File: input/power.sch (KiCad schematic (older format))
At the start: 61 parts, among them Q2 2STD1665T4, Q3 NSS1C300ET4G, U4 OPA830, U6 OPA830, U7 MCP1755S-3302E/DB, U8 NCP1117STAT3G

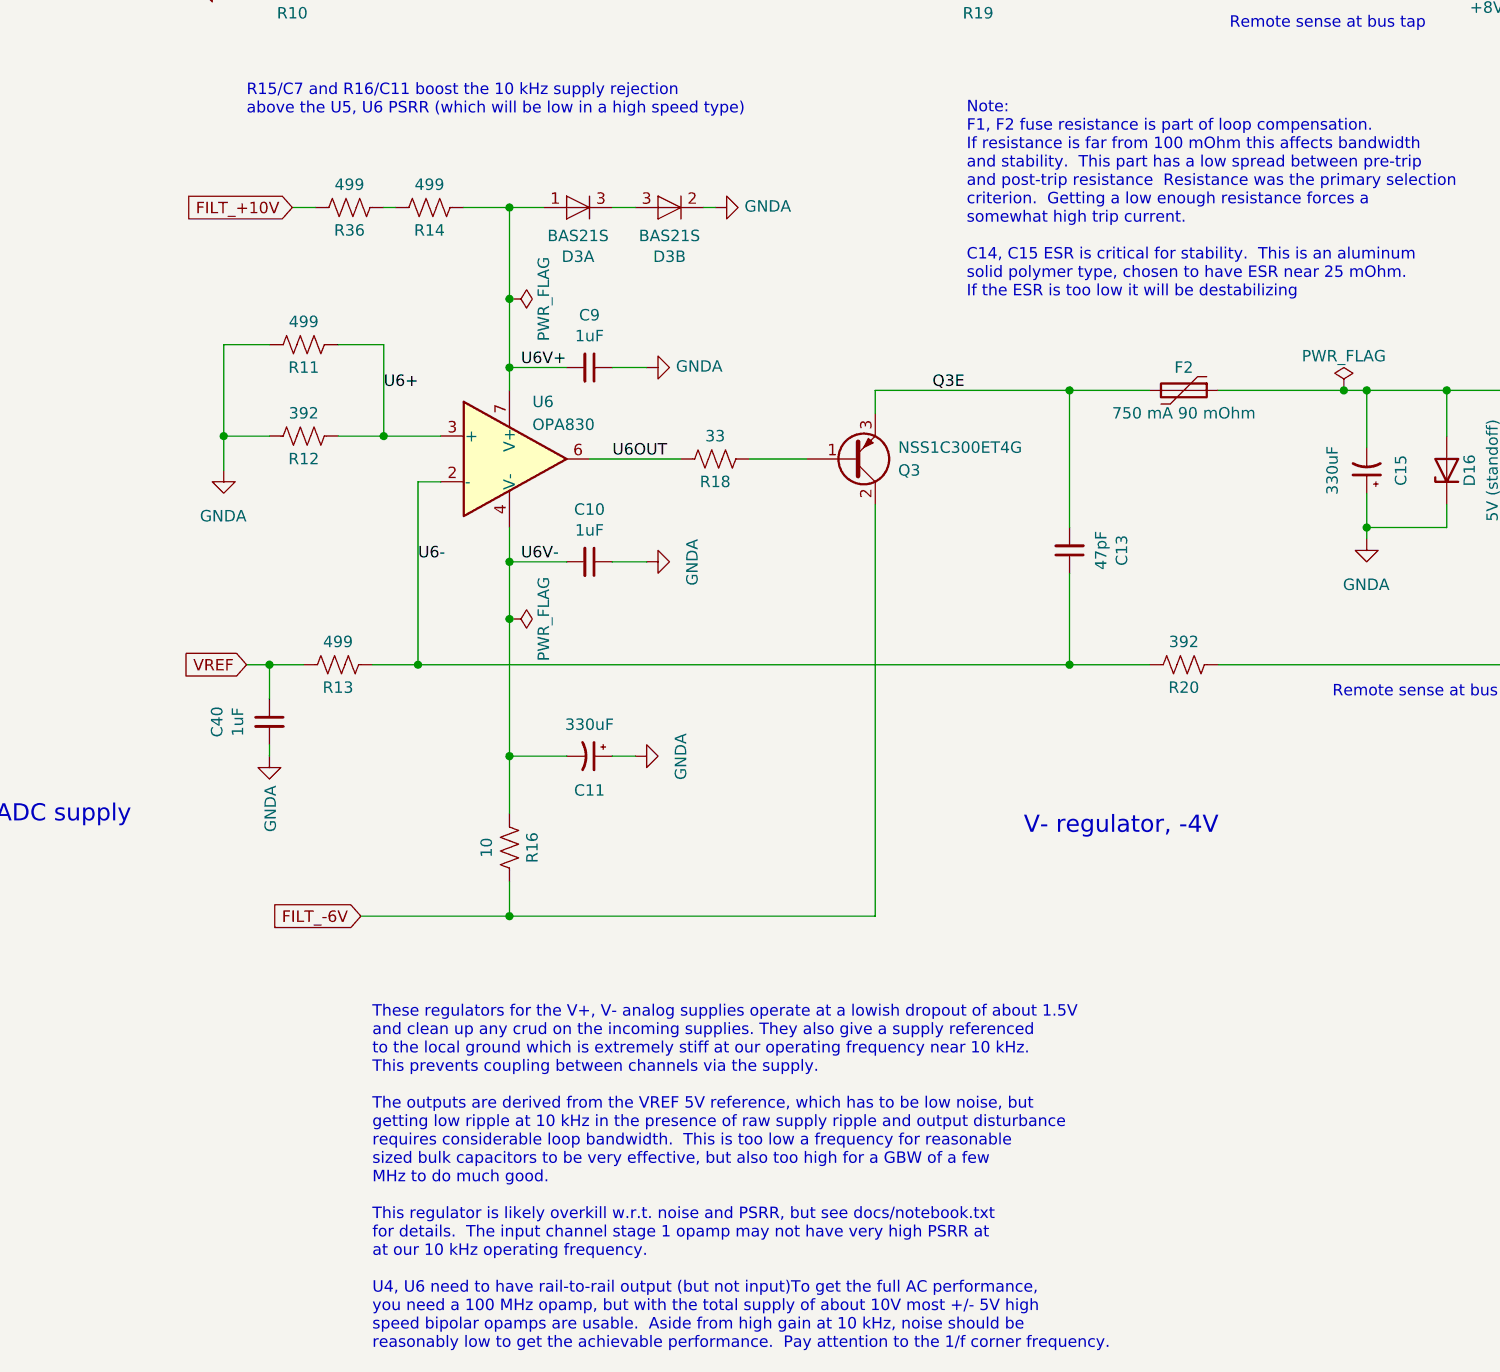
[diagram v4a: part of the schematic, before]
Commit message: Add lowpass filter to input board reference buffer, and fix antialias frequency response. Supply and reference testing in notebook.txt, lots of discussion of reference noise.
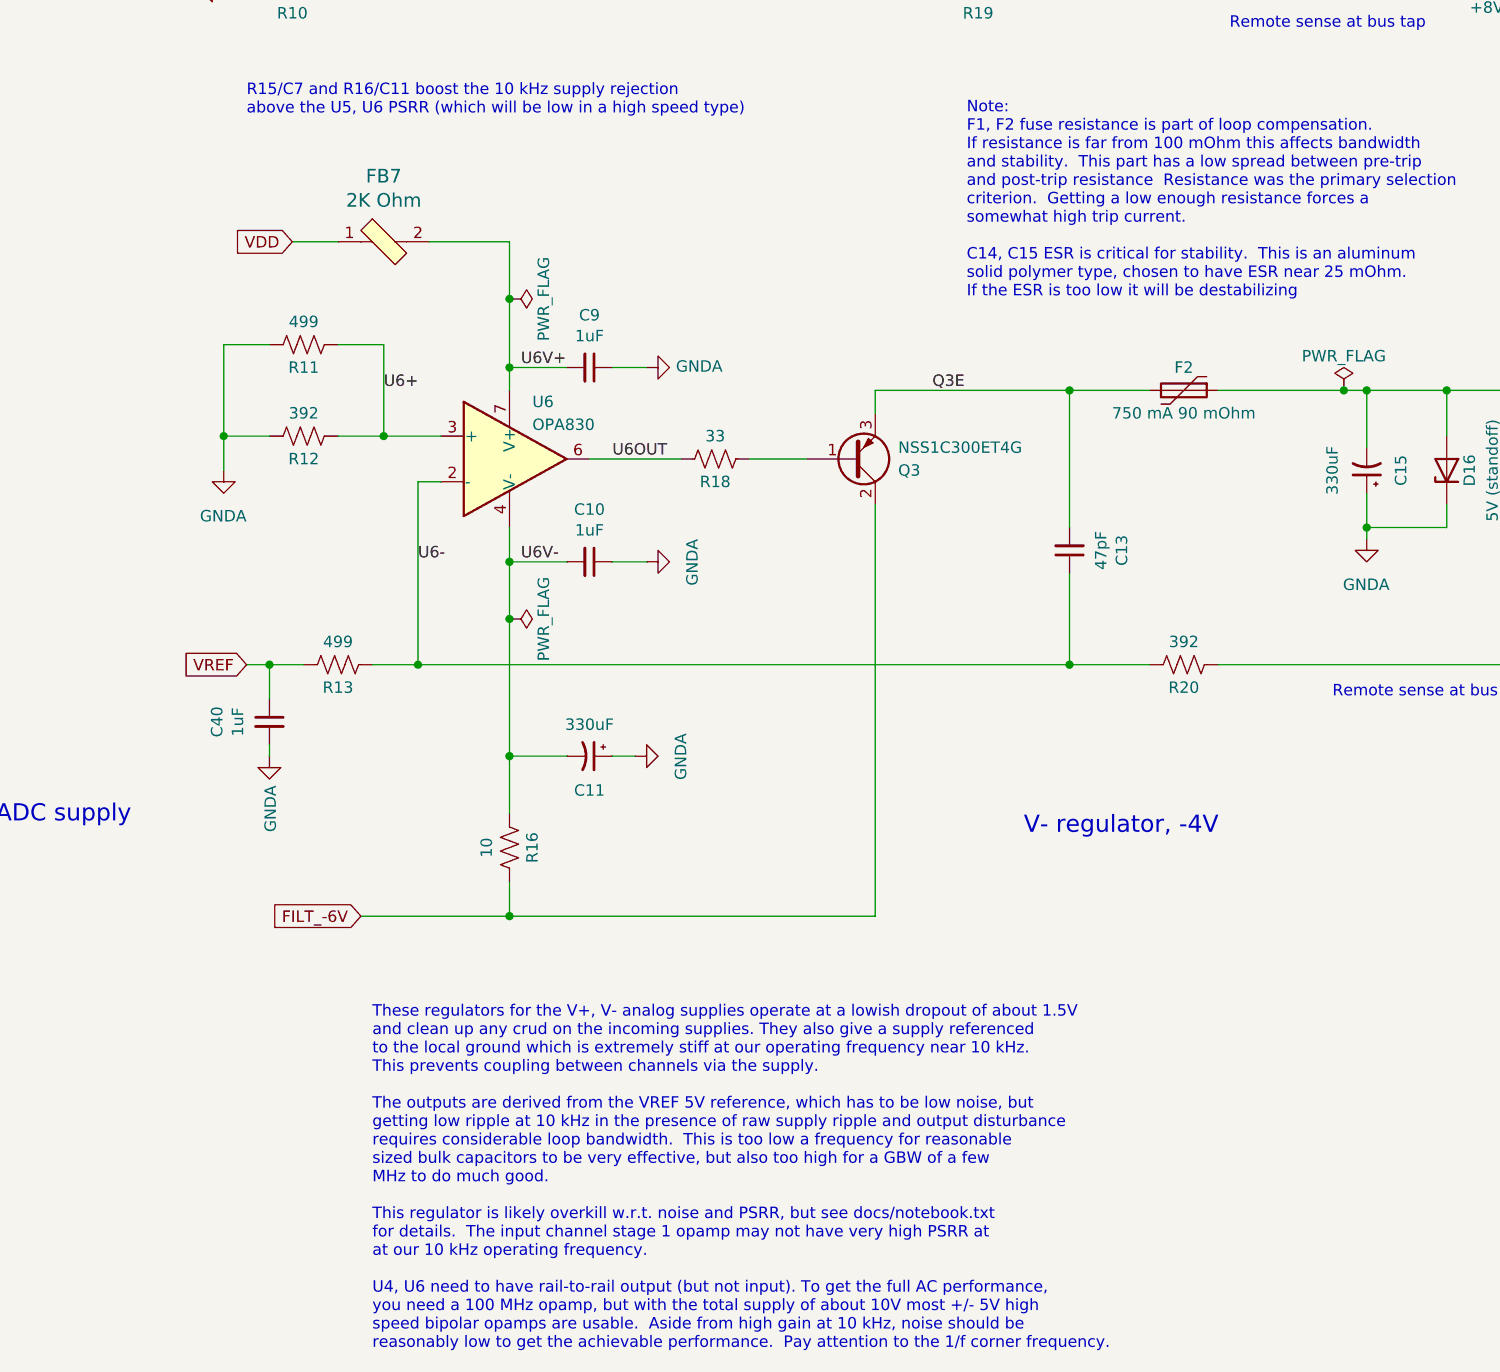
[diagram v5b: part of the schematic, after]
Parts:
- removed D3: BAS21S, Package_TO_SOT_SMD:SOT-23, symbol ilemt_input:BAS21S
- removed R14, R36: 499, Resistor_SMD:R_0805_2012Metric, symbol Device:R_US
- added FB7: 2K Ohm, Inductor_SMD:L_0805_2012Metric, symbol dk_Ferrite-Beads-and-Chips:MPZ2012S601AT000
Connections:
- net U6V+: now also FB7.2
- net VDD: now also FB7.1

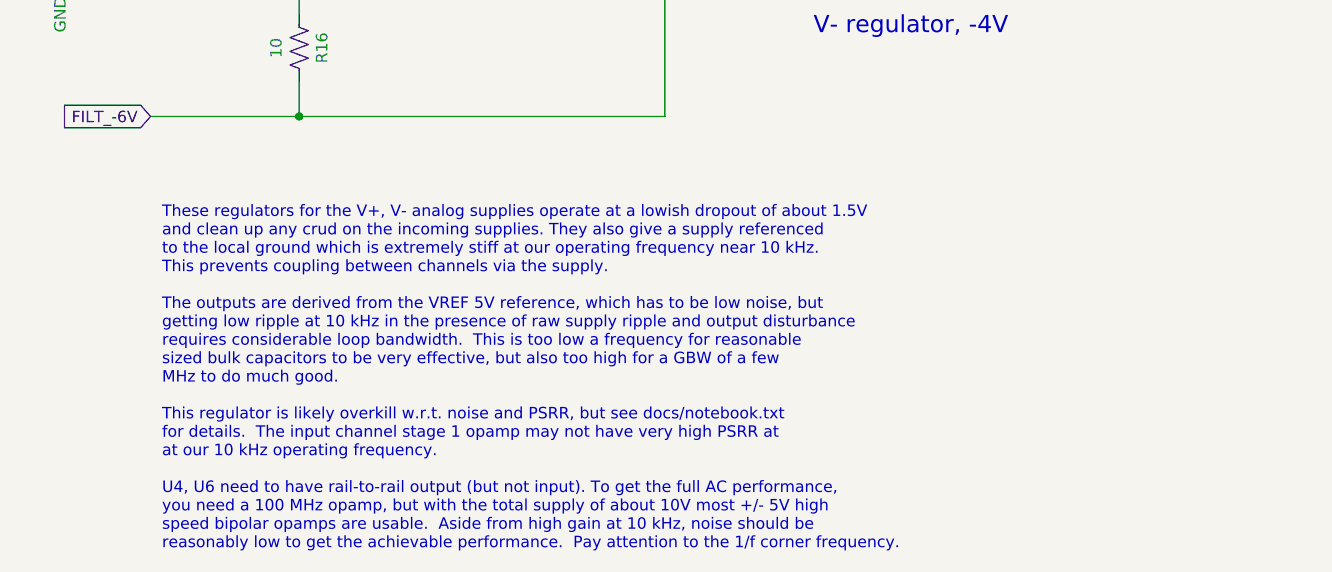
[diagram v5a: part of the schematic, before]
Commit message: notebook.txt and tweaks to comments in input board (no circuit changes).
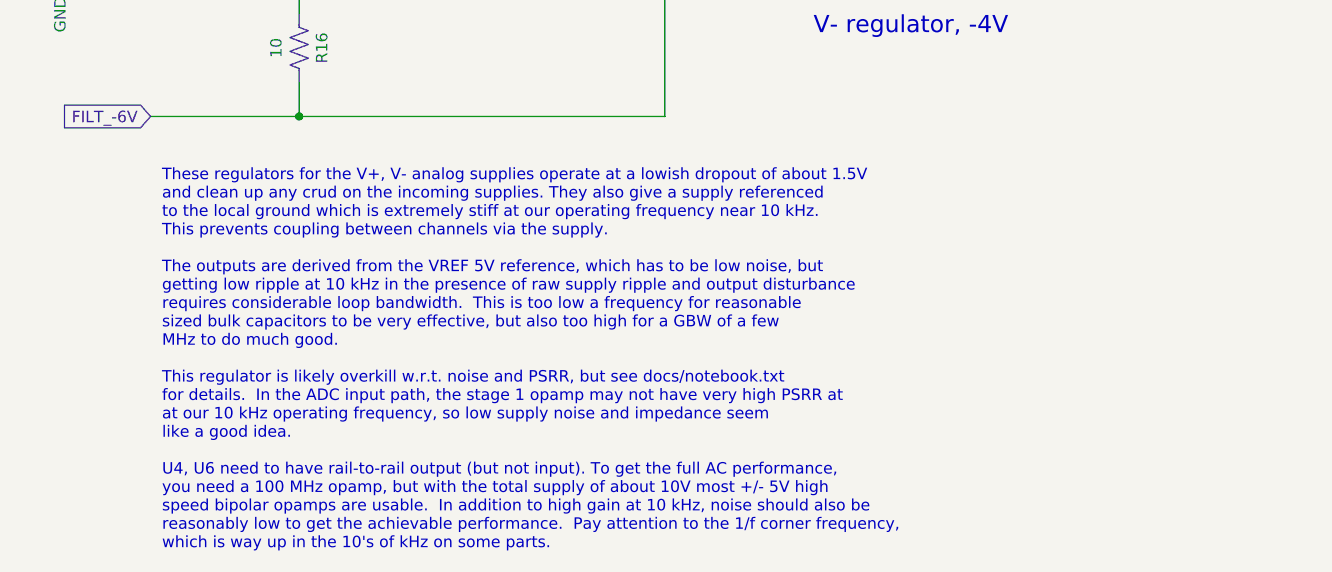
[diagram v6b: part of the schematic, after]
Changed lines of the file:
@@
 $EndComp
 Text Notes 8050 9450 0    50   ~ 0
-These regulators for the V+, V- analog supplies operate at a lowish dropout of about 1.5V\nand clean up any crud on the incoming supplies. They also give a supply referenced\nto the local ground which is extremely stiff at our operating frequency near 10 kHz.\nThis prevents coupling between channels via the supply. \n\nThe outputs are derived from the VREF 5V reference, which has to be low noise, but \ngetting low ripple at 10 kHz in the presence of raw supply ripple and output disturbance\nrequires considerable loop bandwidth.  This is too low a frequency for reasonable\nsized bulk capacitors to be very effective, but also too high for a GBW of a few\nMHz to do much good.\n\nThis regulator is likely overkill w.r.t. noise and PSRR, but see docs/notebook.txt\nfor details.  The input channel stage 1 opamp may not have very high PSRR at\nat our 10 kHz operating frequency.\n\nU4, U6 need to have rail-to-rail output (but not input). To get the full AC performance, \nyou need a 100 MHz opamp, but with the total supply of about 10V most +/- 5V high \nspeed bipolar opamps are usable.  Aside from high gain at 10 kHz, noise should be\nreasonably low to get the achievable performance.  Pay attention to the 1/f corner frequency.\n
+These regulators for the V+, V- analog supplies operate at a lowish dropout of about 1.5V\nand clean up any crud on the incoming supplies. They also give a supply referenced\nto the local ground which is extremely stiff at our operating frequency near 10 kHz.\nThis prevents coupling between channels via the supply. \n\nThe outputs are derived from the VREF 5V reference, which has to be low noise, but \ngetting low ripple at 10 kHz in the presence of raw supply ripple and output disturbance\nrequires considerable loop bandwidth.  This is too low a frequency for reasonable\nsized bulk capacitors to be very effective, but also too high for a GBW of a few\nMHz to do much good.\n\nThis regulator is likely overkill w.r.t. noise and PSRR, but see docs/notebook.txt\nfor details.  In the ADC input path, the stage 1 opamp may not have very high PSRR at\nat our 10 kHz operating frequency, so low supply noise and impedance seem \nlike a good idea.\n\nU4, U6 need to have rail-to-rail output (but not input). To get the full AC performance, \nyou need a 100 MHz opamp, but with the total supply of about 10V most +/- 5V high \nspeed bipolar opamps are usable.  In addition to high gain at 10 kHz, noise should also be\nreasonably low to get the achievable performance.  Pay attention to the 1/f corner frequency,\nwhich is way up in the 10's of kHz on some parts.\n
 Text Notes 10900 7200 0    75   ~ 0
 V- regulator, -4V

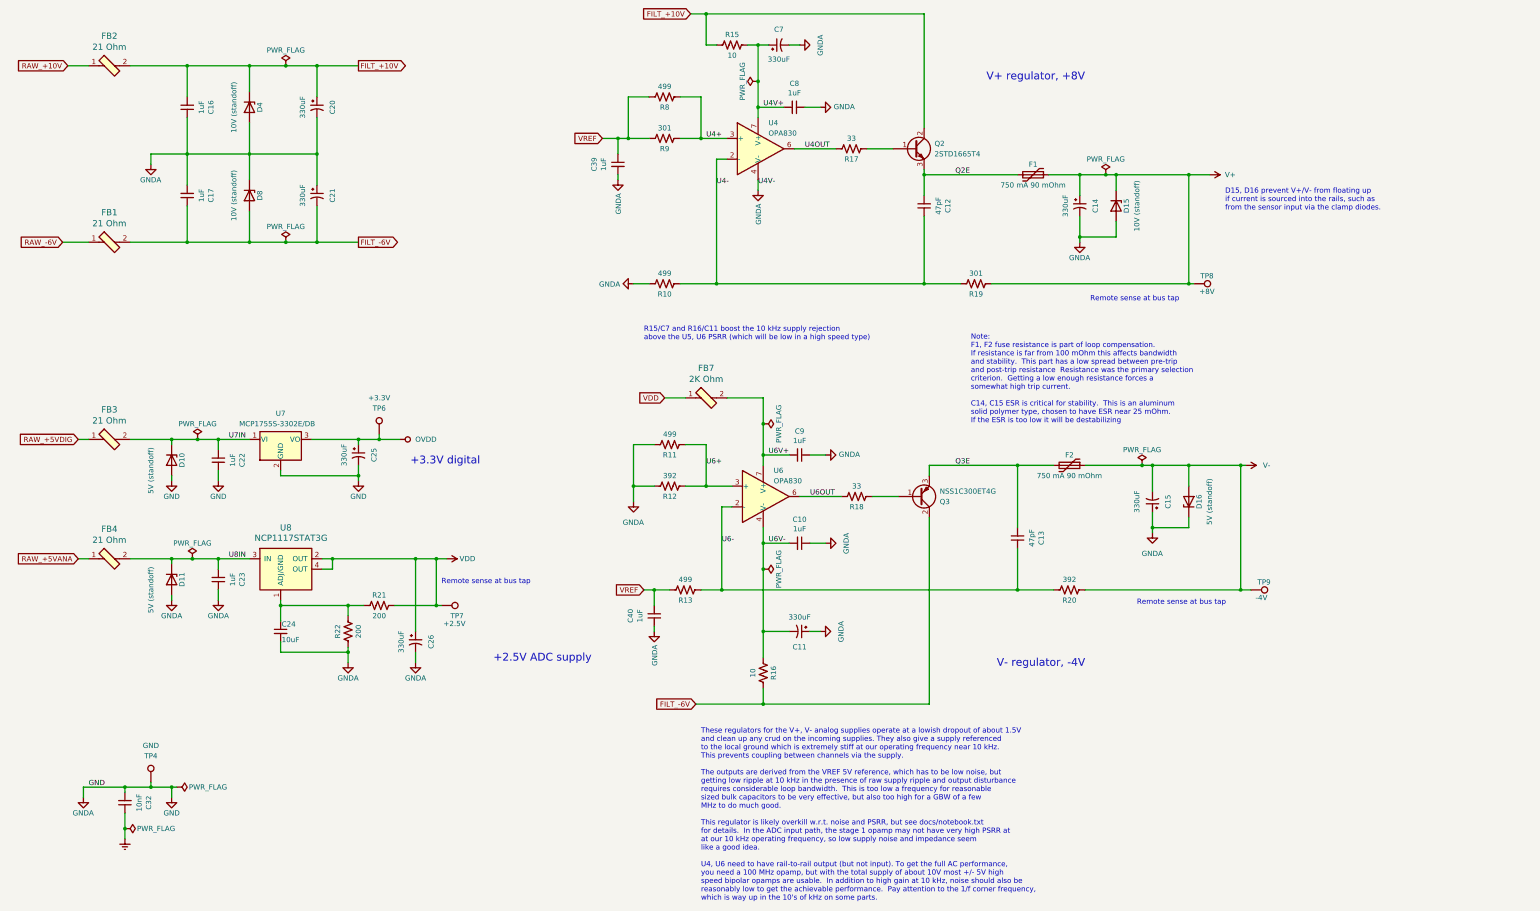
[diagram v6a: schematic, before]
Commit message: BOM change to dac/, start of board revision in input/adc.sch
dac: changed 10 Ohm MPN on BOM

input:
Fixed SOIC-8 footprints
Got rid of bootstrapping of the reference buffer.  Now it runs from the 10 Ohm/330 uF filtered +8/-6.
Changed power input beads from 22 Ohm to 180 Ohm.
Added diode clamp between GND and Earth grounds.
Changed reference buffer to dual opamp.
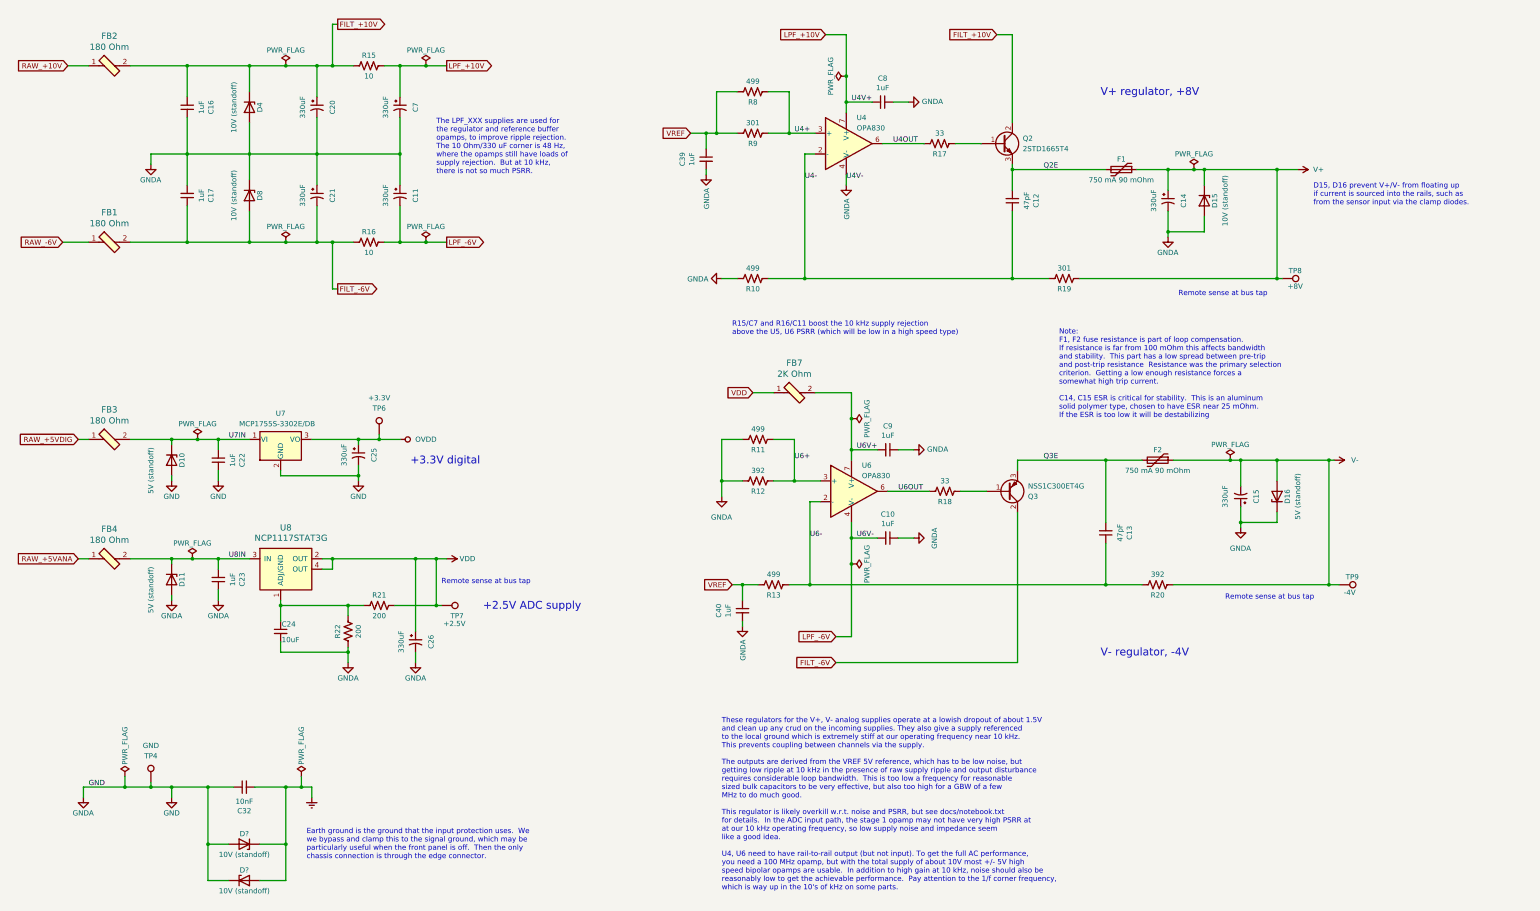
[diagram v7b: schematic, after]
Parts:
- added D? (x2): 10V (standoff), Diode_SMD:D_SMA, symbol Device:D_Zener
- FB1, FB2, FB3, FB4: value 21 Ohm -> 180 Ohm; DK line 24 -> M.36; Description FERRITE BEAD 21 OHM 0805, 100 nH, 5 mOhm -> FERRITE BEAD 180 OHM 0805 1LN; Digikey 587-1765-1-ND -> 732-6123-1-ND; MPN FBMJ2125HM210NT -> 74279220181; Manufacturer Taiyo Yuden -> Würth Elektronik
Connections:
- net Earth: now also C32.2, D?.1 (K), D?.2 (A); no longer C32.1
- net FILT_-6V: now also R16.1; no longer R16.2
- net GND: now also C32.1, D?.1 (K), D?.2 (A); no longer C32.2
- net U4V+ renamed LPF_+10V
- net U6V- renamed LPF_-6V
- net LPF_-6V: now also R16.2; no longer R16.1
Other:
- note added: "Earth ground is the ground that the input protection uses. We\nwe bypass and clamp this to the signal ground, which may be\nparticularly useful when the front panel is off. Then the only\nchassis connection is through the edge connector.\n"
- note added: "The LPF_XXX supplies are used for\nthe regulator and reference buffer\nopamps, to improve ripple rejection.\nThe 10 Ohm/330 uF corner is 48 Hz,\nwhere the opamps still have loads of \nsupply rejection. But at 10 kHz, \nthere is not so much PSRR."
- moved on the sheet: C10, C11, C12, C13, C14, C15, C32, C39, C40, C7, C8, C9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
